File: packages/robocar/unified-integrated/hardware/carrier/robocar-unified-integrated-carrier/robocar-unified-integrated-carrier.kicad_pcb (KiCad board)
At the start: 2 copper layers, 94 x 76 mm, 78 parts, among them J1 IDC 2x7 head cable, J11 Test: 3V3 5V GND VBAT, J12 Test: GND SDA SCL RST, J13 GND post, J14 GND post, J15 UART0 TX tap, J18 GPIO A/B, J19 Speaker, J2 IDC 2x7 head cable, J20 Pan servo (SG90), J21 Tilt servo (SG90), J22 Left RGB LED, J23 Right RGB LED, J3 XT30 pack in, J5 Motor left, J6 Motor right, J7 RCWL-1601 front, J8 RCWL-1601 rear, J9 SSD1306 0.91in, U1 XIAO ESP32-S3 Sense, U10 TPS563201, U2 AMS1117-3.3, U5 TCA9548APWR, U6 PCA9685PW, U7 TB6612FNG, U8 MAX98357AETE+, U9 MCP23017-E/SS

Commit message: feat(robocar-unified-integrated): 5V trunk and pour, SMD bulk capacitors
- 1.5 mm 5V trunk from L1 to C2 beside the TB6612FNG's VM pins, inside a
  +5V pour on F.Cu above GND; B.Cu stays the GND plane.
- Buck GND as a fixed track from U10's GND pin, under the package, to
  input capacitor C11; C9-C11 turned so their GND pads face it.
- C1-C3 470 uF electrolytics become 22 uF MnO2 tantalums (3528): TI caps
  the TPS563201's low-ESR output capacitance at 68 uF, and their ESR
  keeps them out of the D-CAP2 loop and damps FB1. Low-ESR polymer was
  rejected for the same reason.
- C19 100 uF electrolytic on VBAT for hot-plug damping.
- R12 54.9k per SLVSD90B Table 7-2 (4.98 V).
- Floorplan: PCA9685 and its headers swapped with the motor driver block.

Main-board courtyards: 2234 mm^2 (-58 % against the socketed carrier).

Co-Authored-By: Claude Opus 5.5 <noreply@anthropic.com>
Claude-Session: https://claude.ai/code/session_01AoNL8UeiSeWCVt1Bs1JLVr
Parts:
- added C19: 100uF 25V, Capacitor_SMD:CP_Elec_6.3x7.7, F.Cu at (131.3, 156.0)
- C1, C2, C3: value 470uF 16V -> 22uF 16V; footprint Capacitor_SMD:CP_Elec_8x10.5 -> Capacitor_Tantalum_SMD:CP_EIA-3528-21_Kemet-B_HandSolder
- R12: value 56.2k -> 54.9k
- moved C1 28.6 mm to (109.8, 136.0), turned to 90 degrees
- moved J6 22.0 mm to (103.5, 149.0)
- moved J20 21.0 mm to (102.5, 123.0)
- moved J21 21.0 mm to (106.3, 123.0)
- moved J5 20.0 mm to (103.5, 158.0)
- moved J22 19.5 mm to (102.5, 133.5)
- moved J23 19.5 mm to (106.3, 133.5)
- moved C2 19.4 mm to (124.6, 151.5), turned to 90 degrees
- moved U7 16.0 mm to (115.0, 149.0)
- moved C15 15.5 mm to (121.6, 146.5)
- moved C16 15.5 mm to (121.6, 151.0)
- moved R17 13.6 mm to (113.4, 127.5), turned to 180 degrees
- moved R18 13.6 mm to (113.4, 129.6), turned to 180 degrees
- moved R19 13.6 mm to (113.4, 131.7), turned to 180 degrees
- moved R20 13.6 mm to (113.4, 133.8), turned to 180 degrees
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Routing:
- net +3V3: track 312.9 -> 283.3 mm
- net +5V: track 193.8 -> 217.1 mm, vias 7 -> 4
- net PWMA: track 33.6 -> 12.1 mm
- net I2C_SDA: track 45.5 -> 61.4 mm, vias 4 -> 0
- net EXP_GPB7: track 39.8 -> 24.4 mm
- net CH2_SDA: track 53.9 -> 39.8 mm
- net SERVO_PAN: track 36.2 -> 23.7 mm, vias 1 -> 2
- net CH0_SCL: track 48.3 -> 36.2 mm
- net CH3_SCL: track 34.3 -> 44.5 mm, vias 1 -> 2
- net LED_R_G: track 17.1 -> 7.21 mm, vias 1 -> 0
- net LED_L_B: track 27.8 -> 18.7 mm, vias 1 -> 0
- net BIN1: track 27.1 -> 18.1 mm
- net HEAD_I2S_BCLK: track 31.2 -> 22.5 mm, vias 3 -> 0
- net BUCK_FB: track 23.6 -> 15.0 mm
- net LED_R_R: track 15.3 -> 7.18 mm, vias 1 -> 0
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- added copper zone on F.Cu, net +5V

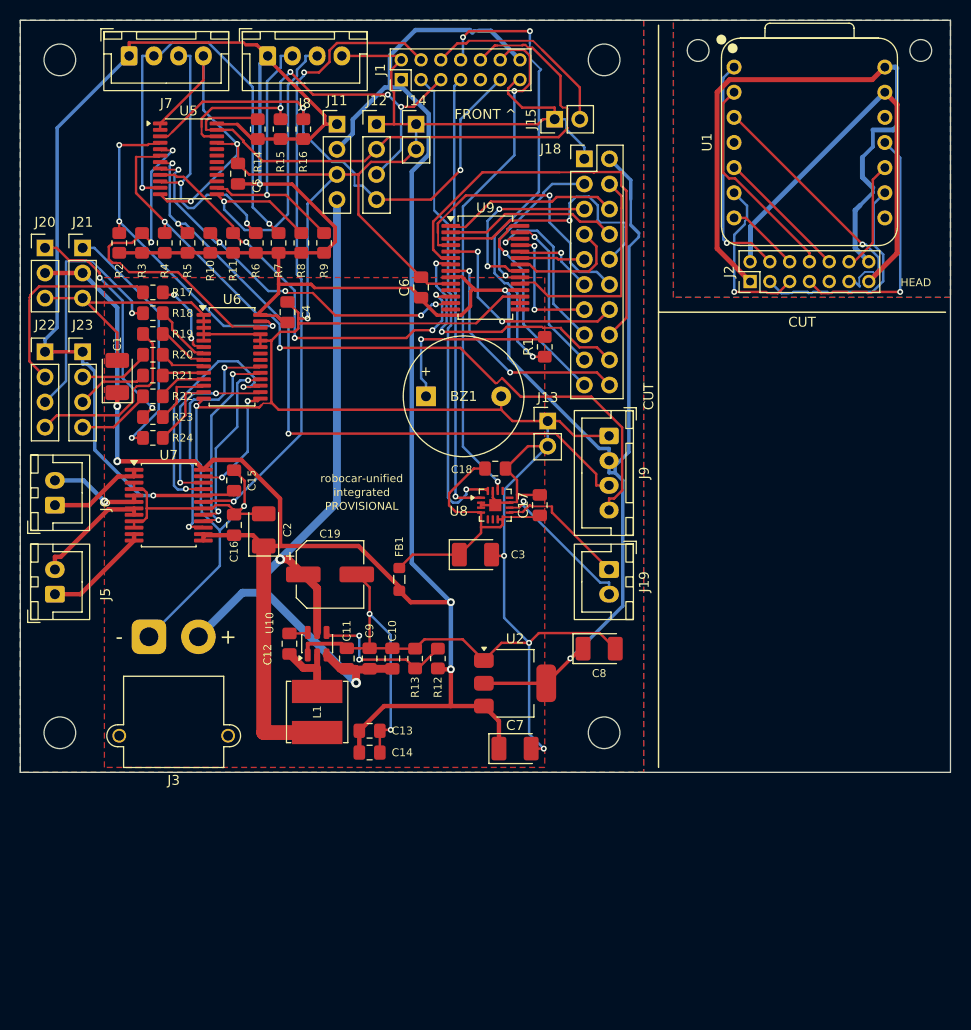
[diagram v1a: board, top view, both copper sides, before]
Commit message: feat(robocar-unified-integrated): add the two spare head boards
The socketed carrier's three head boards, in the same column moved 6 mm
left: head 1 (U1/J2, header on the back), head 2 (U3/J16, front) and
head 3 (U4/J17, back at the top), with M2 holes H5-H10 and each head's
own ground pour (HEAD_GND, HEAD2_GND, HEAD3_GND). The outline grows to
94 x 100 mm; the main board stays 64.5 x 76 and the strip below it is
waste behind a keepout and a cut line.

Co-Authored-By: Claude Opus 5.5 <noreply@anthropic.com>
Claude-Session: https://claude.ai/code/session_01AoNL8UeiSeWCVt1Bs1JLVr
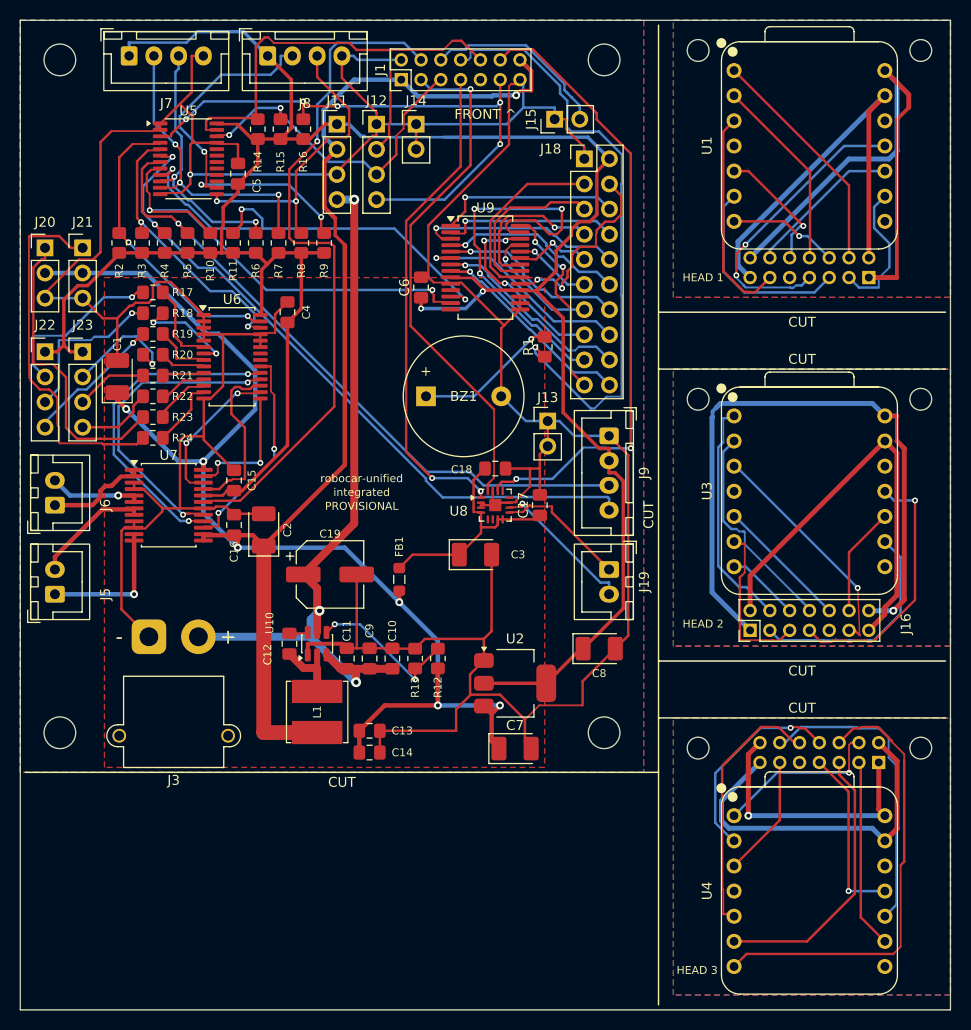
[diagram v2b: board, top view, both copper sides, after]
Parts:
- added H10: M2, MountingHole:MountingHole_2.2mm_M2_ISO7380, F.Cu at (191.0, 173.6)
- added H7: M2, MountingHole:MountingHole_2.2mm_M2_ISO7380, F.Cu at (168.5, 138.3)
- added H8: M2, MountingHole:MountingHole_2.2mm_M2_ISO7380, F.Cu at (191.0, 138.3)
- added H9: M2, MountingHole:MountingHole_2.2mm_M2_ISO7380, F.Cu at (168.5, 173.6)
- added J16: IDC 2x7 head cable, Connector_PinHeader_2.00mm:PinHeader_2x07_P2.00mm_Vertical, F.Cu at (173.8, 161.7)
- added J17: IDC 2x7 head cable, Connector_PinHeader_2.00mm:PinHeader_2x07_P2.00mm_Vertical, B.Cu at (186.8, 175.0)
- added U3: XIAO ESP32-S3 Sense, Seeed_XIAO:XIAO-ESP32-S3-Socket, F.Cu at (179.8, 147.6)
- added U4: XIAO ESP32-S3 Sense, Seeed_XIAO:XIAO-ESP32-S3-Socket, F.Cu at (179.8, 188.0)
- J2: moved to B.Cu
- moved J2 12.0 mm to (185.8, 126.0)
- moved U1 0.35 mm to (179.8, 112.7)
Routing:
- net HEAD2_+5V: track 0.00 -> 66.2 mm, vias 0 -> 1
- net HEAD3_UART0_TX: track 0.00 -> 45.7 mm
- net HEAD2_GND: track 0.00 -> 43.6 mm
- net +3V3: track 283.3 -> 244.8 mm, vias 4 -> 2
- net HEAD3_GND: track 0.00 -> 36.1 mm
- net HEAD3_I2S_LRCLK: track 0.00 -> 31.0 mm
- net HEAD3_I2C_SCL: track 0.00 -> 28.1 mm
- net HEAD3_+5V: track 0.00 -> 27.3 mm, vias 0 -> 1
- net HEAD2_I2S_DIN: track 0.00 -> 26.6 mm, vias 0 -> 1
- net HEAD3_I2C_SDA: track 0.00 -> 26.3 mm
- net EXP_GPA6: track 16.2 -> 40.3 mm, vias 1 -> 3
- net HEAD2_MUX_RST: track 0.00 -> 23.7 mm, vias 0 -> 1
- net GND: track 423.6 -> 400.2 mm, vias 10 -> 1
- net HEAD2_MOTOR_STBY: track 0.00 -> 23.4 mm
- net HEAD2_I2S_BCLK: track 0.00 -> 22.7 mm
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- added copper zone on B.Cu, net HEAD2_GND
- added copper zone on F.Cu, net HEAD2_GND
- added copper zone on B.Cu, net HEAD3_GND
- added copper zone on F.Cu, net HEAD3_GND
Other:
- board size 94 x 76 mm -> 94 x 100 mm
- board text added: "HEAD 1"
- board text added: "HEAD 2"
- board text added: "HEAD 3"
- board text removed: "HEAD"

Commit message: fix(robocar-unified-integrated): address the pre-fab review
Layout (review B1): the +5V F.Cu pour cut F.Cu GND into islands around
every chip in the power half, and the board had one GND via, so their
ground pads reached the B.Cu plane through 0.19-0.25 mm tracks. The pour
is gone; [fanout] adds 48 GND vias, required on every power-path pad;
the MAX98357A's GND pins and GAIN_SLOT tie to its exposed pad, which
takes an in-pad via. Pours stop 1 mm short of every cut line.

Power stage:
- TPS563208 (forced-continuous: sinks motor regeneration) for the
  TPS563201; same pins and Table 7-2 values.
- L1 4.7 uH +/-20 % (the 3.3 uH part's +/-30 % can fall below 3.3 uH);
  a third 22 uF output capacitor, C20.
- EN divider R25/R26 (100k/30k): on near 6.2 V, off near 4.9 V.
- F1 3 A PTC between the XT30 and VBAT.

Placement: the EN and feedback dividers beside their pins above U10,
C13/C14/C20 east of L1, FB1 beside the amplifier, C8 beside the LDO,
C7 and C14 away from the y 76 cut. RGB green/blue series 47 ohm.
Silkscreen text 1.0 mm (0.8 mm where it cannot fit), stroke >= 0.16 mm.
Freerouting's neck-downs below the 0.15 mm minimum are widened after
routing. README: the review's open items, the 6.7 V dropout and the 5 V
current budget.

Co-Authored-By: Claude Opus 5.5 <noreply@anthropic.com>
Claude-Session: https://claude.ai/code/session_01AoNL8UeiSeWCVt1Bs1JLVr
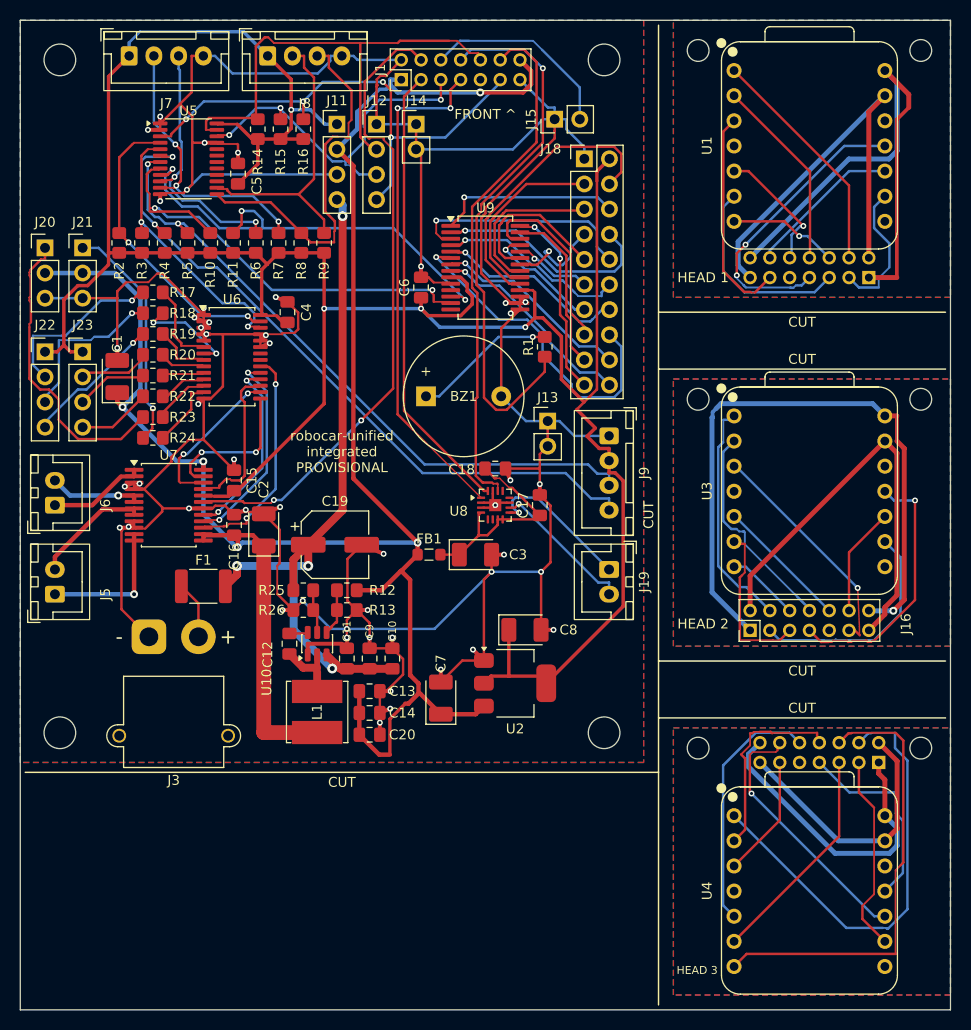
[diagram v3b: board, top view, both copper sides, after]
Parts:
- added C20: 22uF 16V, Capacitor_SMD:C_0805_2012Metric_Pad1.18x1.45mm_HandSolder, F.Cu at (135.3, 172.2)
- added F1: 3A hold 16V, Fuse:Fuse_1812_4532Metric_Pad1.30x3.40mm_HandSolder, F.Cu at (118.5, 157.2)
- added R25: 100k, Resistor_SMD:R_0805_2012Metric_Pad1.20x1.40mm_HandSolder, F.Cu at (128.6, 157.6)
- added R26: 30k, Resistor_SMD:R_0805_2012Metric_Pad1.20x1.40mm_HandSolder, F.Cu at (128.6, 159.6)
- L1: value 3.3uH -> 4.7uH
- R18, R19, R21, R22: value 220 -> 47
- U10: value TPS563201 -> TPS563208
- moved R12 11.5 mm to (133.0, 157.6), turned to 180 degrees
- moved C7 9.07 mm to (142.5, 168.5), turned to 90 degrees
- moved R13 8.46 mm to (133.0, 159.6), turned to 0 degrees
- moved C8 7.74 mm to (151.0, 161.6)
- moved C13 4.00 mm to (135.3, 167.8)
- moved C14 4.00 mm to (135.3, 170.0)
- moved FB1 3.91 mm to (141.3, 154.0), turned to 0 degrees
- moved C19 3.04 mm to (131.8, 153.0)
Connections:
- J3 pad 2: VBAT -> PACK_IN
- U10 pad 5: VBAT -> BUCK_EN
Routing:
- net GND: track 400.2 -> 437.1 mm, vias 1 -> 48
- net HEAD3_MOTOR_STBY: track 17.3 -> 45.5 mm, vias 1 -> 0
- net EXP_GPA6: track 40.3 -> 16.9 mm, vias 3 -> 0
- net +3V3: track 244.8 -> 267.7 mm, vias 2 -> 4
- net SERVO_TILT: track 37.4 -> 23.5 mm, vias 0 -> 1
- net +5V: track 225.0 -> 211.3 mm, vias 7 -> 5
- net BIN2: track 33.0 -> 20.6 mm
- net BIN1: track 31.3 -> 18.8 mm
- net EXP_GPB5: track 22.2 -> 34.1 mm
- net BUCK_FB: track 15.8 -> 4.76 mm, vias 2 -> 0
- net I2S_LRCLK: track 63.7 -> 52.7 mm, vias 2 -> 0
- net CH4_SCL: track 39.7 -> 29.8 mm, vias 3 -> 0
- net EXP_INTB: track 19.8 -> 29.2 mm, vias 2 -> 0
- net HEAD3_GND: track 36.1 -> 27.1 mm
- net EXP_GPA2: track 7.94 -> 16.0 mm, vias 1 -> 0
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- removed copper zone on F.Cu, net +5V

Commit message: feat(robocar-unified-integrated): LCSC parts for every SMD line, fiducials, 2.2k I2C pull-ups
Every SMD part now has an LCSC number (Basic where one exists), so
carrier-fab's bom-jlc.csv and cpl-jlc.csv cover all 56 placements. Three
fiducials on the main board. The I2C pull-ups follow the socketed
carrier's 2.2 kOhm (#810). Board re-placed, re-routed and checked with
KiCad 10.0.6; README records the part table, rotations and a cost estimate.

Refs #808

Co-Authored-By: Claude Opus 5.5 <noreply@anthropic.com>
Claude-Session: https://claude.ai/code/session_01NQBHdVJbY6M136w1wzwDHy
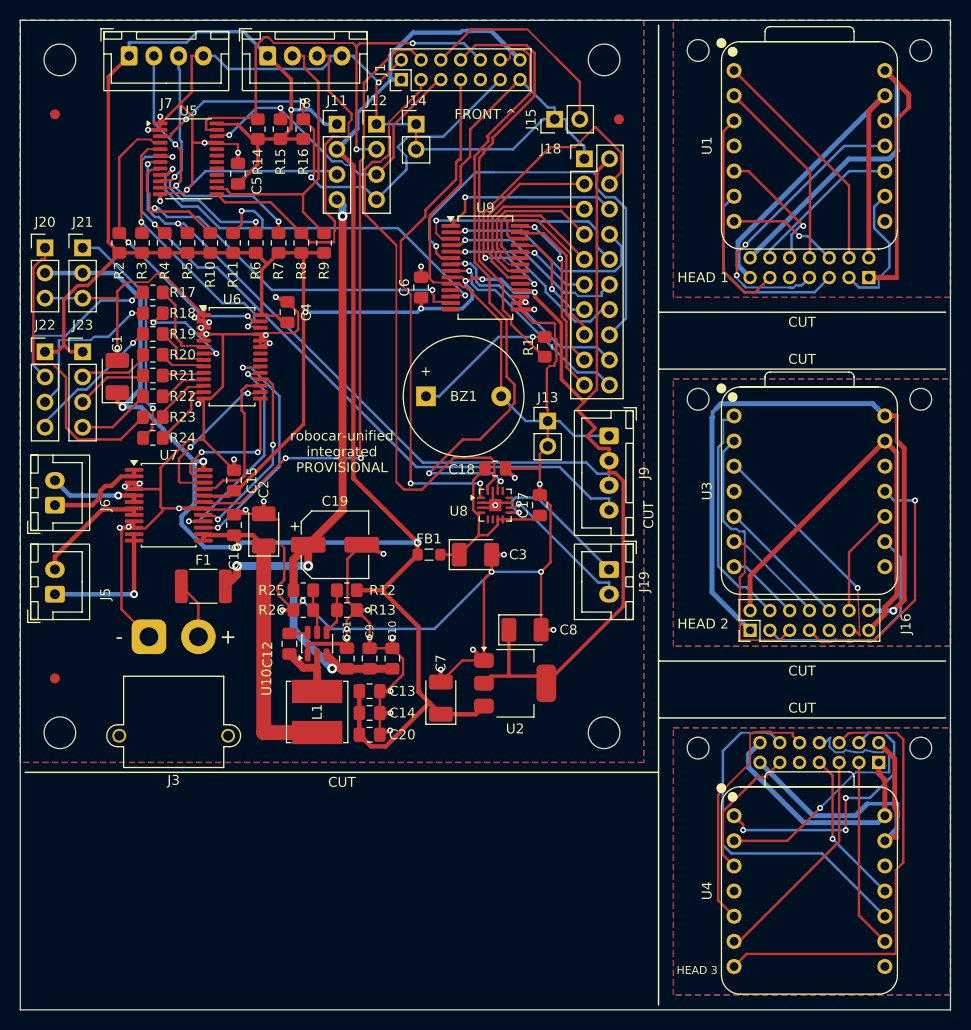
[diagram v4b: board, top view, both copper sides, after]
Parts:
- added FID1: Fiducial, Fiducial:Fiducial_1mm_Mask2mm, F.Cu at (103.5, 109.5)
- added FID2: Fiducial, Fiducial:Fiducial_1mm_Mask2mm, F.Cu at (160.5, 110.0)
- added FID3: Fiducial, Fiducial:Fiducial_1mm_Mask2mm, F.Cu at (103.5, 166.5)
- C13, C14, C20: value 22uF 16V -> 22uF 25V
- C19: value 100uF 25V -> 100uF 35V
- FB1: value 600R@100MHz 2A -> 220R@100MHz 2A
- R10, R11, R14, R15, R2, R3, R4, R5, R6, R7, R8, R9: value 10k -> 2.2k
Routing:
- net HEAD3_MOTOR_STBY: track 45.5 -> 28.9 mm, vias 0 -> 3
- net I2S_BCLK: track 46.0 -> 59.9 mm
- net PIEZO: track 55.7 -> 44.2 mm, vias 1 -> 0
- net I2S_LRCLK: track 52.7 -> 63.8 mm, vias 0 -> 2
- net HEAD3_PIEZO: track 19.9 -> 29.5 mm, vias 0 -> 1
- net HEAD3_I2S_LRCLK: track 26.5 -> 35.8 mm, vias 1 -> 0
- net EXP_GPB5: track 34.1 -> 43.0 mm
- net HEAD3_+5V: track 31.1 -> 25.0 mm
- net EXP_GPA1: track 10.6 -> 16.3 mm, vias 1 -> 0
- net HEAD3_GND: track 27.1 -> 32.6 mm
- net EXP_INTB: track 29.2 -> 34.3 mm, vias 0 -> 2
- net +3V3: track 267.7 -> 262.7 mm, vias 4 -> 6
- net GND: track 437.1 -> 441.9 mm
- net HEAD3_I2S_DIN: track 20.0 -> 15.7 mm, vias 0 -> 1
- net I2C_SCL: track 37.5 -> 33.7 mm, vias 3 -> 2
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
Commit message: feat(robocar-unified-integrated): route and check the mouse-bite board
Placed, routed and checked with KiCad 10.0.6: ERC, DRC with schematic
parity, netlist parity, boardcheck (tabs and slots against [panel]) and the
stamp. The NPTH drill file carries the 140 mouse-bite holes.

Refs #809

Co-Authored-By: Claude Opus 5.5 <noreply@anthropic.com>
Claude-Session: https://claude.ai/code/session_01NQBHdVJbY6M136w1wzwDHy
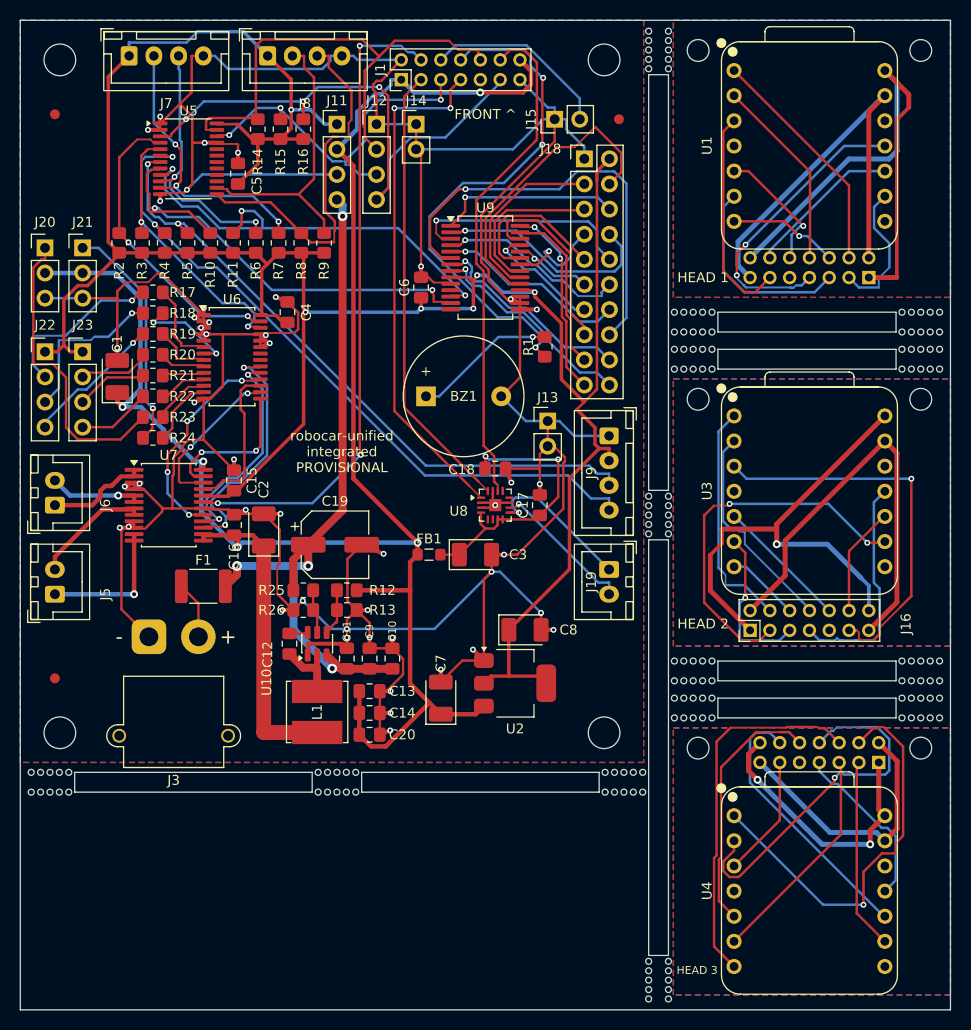
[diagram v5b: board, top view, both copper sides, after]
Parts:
- added MB1: MouseBites, MouseBites, F.Cu at (164.5, 197.0)
- added MB10: MouseBites, MouseBites, F.Cu at (191.0, 134.2)
- added MB11: MouseBites, MouseBites, F.Cu at (191.0, 165.8)
- added MB12: MouseBites, MouseBites, F.Cu at (168.0, 165.8)
- added MB13: MouseBites, MouseBites, F.Cu at (168.0, 169.5)
- added MB14: MouseBites, MouseBites, F.Cu at (191.0, 169.5)
- added MB2: MouseBites, MouseBites, F.Cu at (164.5, 150.0)
- added MB3: MouseBites, MouseBites, F.Cu at (164.5, 103.0)
- added MB4: MouseBites, MouseBites, F.Cu at (161.0, 177.0)
- added MB5: MouseBites, MouseBites, F.Cu at (132.0, 177.0)
- added MB6: MouseBites, MouseBites, F.Cu at (103.0, 177.0)
- added MB7: MouseBites, MouseBites, F.Cu at (191.0, 130.5)
- added MB8: MouseBites, MouseBites, F.Cu at (168.0, 130.5)
- added MB9: MouseBites, MouseBites, F.Cu at (168.0, 134.2)
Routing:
- net HEAD2_+5V: track 66.1 -> 49.0 mm
- net HEAD2_MUX_RST: track 23.7 -> 39.6 mm
- net HEAD2_I2S_BCLK: track 22.7 -> 37.9 mm, vias 0 -> 2
- net I2S_BCLK: track 59.9 -> 45.8 mm
- net I2S_LRCLK: track 63.8 -> 51.4 mm, vias 2 -> 0
- net HEAD3_MOTOR_STBY: track 28.9 -> 41.2 mm, vias 3 -> 1
- net AMP_5V: track 19.8 -> 29.0 mm, vias 0 -> 2
- net HEAD3_UART0_TX: track 46.0 -> 37.3 mm
- net HEAD3_I2S_LRCLK: track 35.8 -> 27.3 mm
- net PIEZO: track 44.2 -> 52.6 mm, vias 0 -> 3
- net HEAD3_PIEZO: track 29.5 -> 36.7 mm
- net MUX_RST: track 51.9 -> 57.7 mm
- net EXP_GPA1: track 16.3 -> 10.6 mm, vias 0 -> 1
- net HEAD3_GND: track 32.6 -> 27.1 mm
- net +3V3: track 262.7 -> 258.2 mm
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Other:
- outline, holes or cut-outs redrawn
- board text removed: "CUT"
